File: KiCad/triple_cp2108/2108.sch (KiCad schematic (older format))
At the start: 79 parts, among them IC1 CP2108-B03-GMR, J19 Screw_Terminal_01x09, J20 Screw_Terminal_01x09, J21 Screw_Terminal_01x09, J22 Screw_Terminal_01x09, J23 RJ12, J24 RJ12, J25 RJ12, J26 RJ12, J28 DB9_Male, J29 DB9_Male, J30 DB9_Male, J31 DB9_Male, U11 SP3243, U12 SP3243, U13 SP3243, U14 SP3243

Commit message: Netlist generated
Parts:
- removed J19, J20, J21, J22: Screw_Terminal_01x09, Connector_PinHeader_1.00mm:PinHeader_1x09_P1.00mm_Horizontal, symbol Connector:Screw_Terminal_01x09
- C11: renamed from C69; footprint (none) -> Capacitor_SMD:C_0805_2012Metric_Pad1.18x1.45mm_HandSolder
- C16: renamed from C71; footprint (none) -> Capacitor_SMD:C_0805_2012Metric_Pad1.18x1.45mm_HandSolder
- C9: renamed from C67; footprint (none) -> Capacitor_SMD:C_0805_2012Metric_Pad1.18x1.45mm_HandSolder
- J4: renamed from J23; footprint (none) -> Connector_RJ:RJ12_Amphenol_54601
- J5: renamed from J25; footprint (none) -> Connector_RJ:RJ12_Amphenol_54601
- J6: renamed from J24; footprint (none) -> Connector_RJ:RJ12_Amphenol_54601
- J7: renamed from J26; footprint (none) -> Connector_RJ:RJ12_Amphenol_54601
- R10: renamed from R57; footprint Resistor_SMD:R_1206_3216Metric -> Resistor_SMD:R_0805_2012Metric_Pad1.20x1.40mm_HandSolder
- R11: renamed from R74; footprint Resistor_SMD:R_1206_3216Metric -> Resistor_SMD:R_0805_2012Metric_Pad1.20x1.40mm_HandSolder
- R12: renamed from R58; footprint Resistor_SMD:R_1206_3216Metric -> Resistor_SMD:R_0805_2012Metric_Pad1.20x1.40mm_HandSolder
- R13: renamed from R75; footprint Resistor_SMD:R_1206_3216Metric -> Resistor_SMD:R_0805_2012Metric_Pad1.20x1.40mm_HandSolder
- R14: renamed from R59; footprint Resistor_SMD:R_1206_3216Metric -> Resistor_SMD:R_0805_2012Metric_Pad1.20x1.40mm_HandSolder
- R15: renamed from R76; footprint Resistor_SMD:R_1206_3216Metric -> Resistor_SMD:R_0805_2012Metric_Pad1.20x1.40mm_HandSolder
- R16: renamed from R60; footprint Resistor_SMD:R_1206_3216Metric -> Resistor_SMD:R_0805_2012Metric_Pad1.20x1.40mm_HandSolder
- R17: renamed from R77; footprint Resistor_SMD:R_1206_3216Metric -> Resistor_SMD:R_0805_2012Metric_Pad1.20x1.40mm_HandSolder
- R18: renamed from R61; footprint Resistor_SMD:R_1206_3216Metric -> Resistor_SMD:R_0805_2012Metric_Pad1.20x1.40mm_HandSolder
- R19: renamed from R78; footprint Resistor_SMD:R_1206_3216Metric -> Resistor_SMD:R_0805_2012Metric_Pad1.20x1.40mm_HandSolder
- R20: renamed from R62; footprint Resistor_SMD:R_1206_3216Metric -> Resistor_SMD:R_0805_2012Metric_Pad1.20x1.40mm_HandSolder
- R21: renamed from R79; footprint Resistor_SMD:R_1206_3216Metric -> Resistor_SMD:R_0805_2012Metric_Pad1.20x1.40mm_HandSolder
- R22: renamed from R64; value R -> 100; footprint Resistor_SMD:R_1206_3216Metric -> Resistor_SMD:R_0805_2012Metric_Pad1.20x1.40mm_HandSolder
- R23: renamed from R65; value R -> 100; footprint Resistor_SMD:R_1206_3216Metric -> Resistor_SMD:R_0805_2012Metric_Pad1.20x1.40mm_HandSolder
- R24: renamed from R66; value R -> 100; footprint Resistor_SMD:R_1206_3216Metric -> Resistor_SMD:R_0805_2012Metric_Pad1.20x1.40mm_HandSolder
- R25: renamed from R67; value R -> 100; footprint Resistor_SMD:R_1206_3216Metric -> Resistor_SMD:R_0805_2012Metric_Pad1.20x1.40mm_HandSolder
- R26: renamed from R68; value R -> 100; footprint Resistor_SMD:R_1206_3216Metric -> Resistor_SMD:R_0805_2012Metric_Pad1.20x1.40mm_HandSolder
- R27: renamed from R69; value R -> 100; footprint Resistor_SMD:R_1206_3216Metric -> Resistor_SMD:R_0805_2012Metric_Pad1.20x1.40mm_HandSolder
- R28: renamed from R70; value R -> 100; footprint Resistor_SMD:R_1206_3216Metric -> Resistor_SMD:R_0805_2012Metric_Pad1.20x1.40mm_HandSolder
- R29: renamed from R71; value R -> 100; footprint Resistor_SMD:R_1206_3216Metric -> Resistor_SMD:R_0805_2012Metric_Pad1.20x1.40mm_HandSolder
- R5: renamed from R55; footprint Resistor_SMD:R_1206_3216Metric -> Resistor_SMD:R_0805_2012Metric_Pad1.20x1.40mm_HandSolder
- R6: renamed from R72; footprint Resistor_SMD:R_1206_3216Metric -> Resistor_SMD:R_0805_2012Metric_Pad1.20x1.40mm_HandSolder
- R7: renamed from R63; footprint Resistor_SMD:R_1206_3216Metric -> Resistor_SMD:R_0805_2012Metric_Pad1.20x1.40mm_HandSolder
- R8: renamed from R56; footprint Resistor_SMD:R_1206_3216Metric -> Resistor_SMD:R_0805_2012Metric_Pad1.20x1.40mm_HandSolder
- R9: renamed from R73; footprint Resistor_SMD:R_1206_3216Metric -> Resistor_SMD:R_0805_2012Metric_Pad1.20x1.40mm_HandSolder
- U3: renamed from U11; Manufacturer_Part_Number (none) -> SP3243EUEY-L/TR; Mouser Price/Stock (none) -> https://lcsc.com/product-detail/RS232-ICs_MaxLinear_SP3243E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
- U4: renamed from U12; Manufacturer_Part_Number (none) -> SP3243EUEY-L/TR; Mouser Price/Stock (none) -> https://lcsc.com/product-detail/RS232-ICs_MaxLinear_SP3243E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
- U5: renamed from U13; Manufacturer_Part_Number (none) -> SP3243EUEY-L/TR; Mouser Price/Stock (none) -> https://lcsc.com/product-detail/RS232-ICs_MaxLinear_SP3243E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
- U6: renamed from U14; Manufacturer_Part_Number (none) -> SP3243EUEY-L/TR; Mouser Price/Stock (none) -> https://lcsc.com/product-detail/RS232-ICs_MaxLinear_SP3243E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
- renumbered C68 to C10, C72 to C12, C73 to C13, C74 to C14, C70 to C15, C75 to C17, C76 to C18, C77 to C19, C78 to C20, C79 to C21, C80 to C22, C81 to C23, C82 to C24, C83 to C25, C84 to C26, C85 to C27, C86 to C28, C87 to C29, C88 to C30, C89 to C31, C90 to C32, C91 to C33, C92 to C34, C93 to C35, C94 to C36, C66 to C8, D19 to D13, D20 to D14, D21 to D15, D22 to D16, D23 to D17, D24 to D18, D25 to D19, D26 to D20, J30 to J10, J31 to J11, J28 to J8, J29 to J9
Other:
- moved on the sheet: J4, J5, J6, J7, R10, R11, R12, R13, R14, R15, R16, R17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

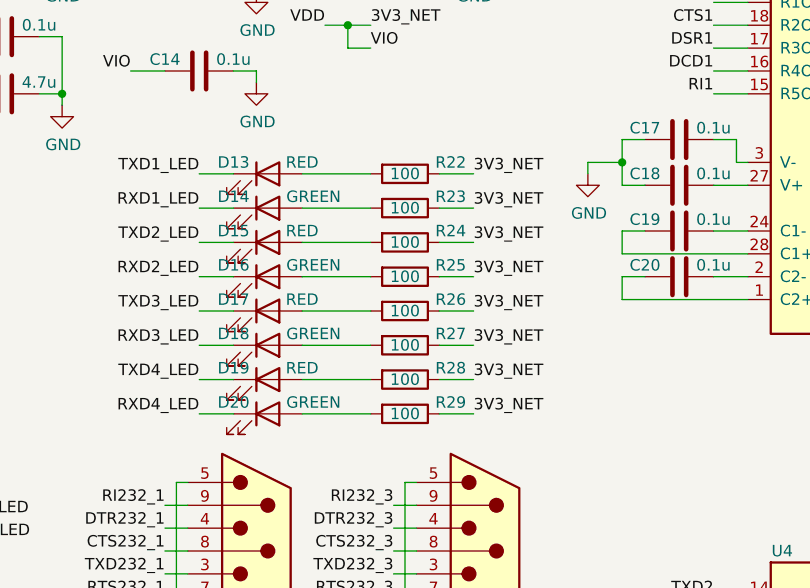
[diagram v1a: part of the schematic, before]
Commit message: LED resis val changed
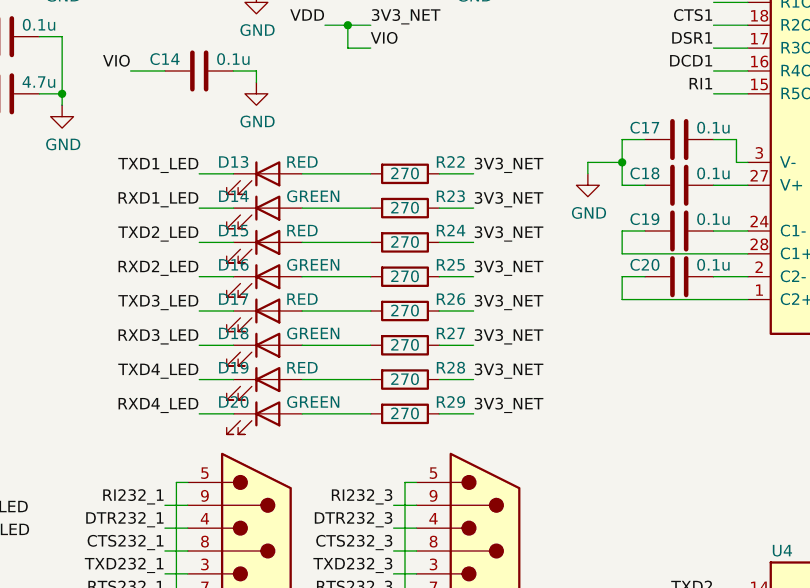
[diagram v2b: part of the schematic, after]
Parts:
- R22, R23, R24, R25, R26, R27, R28, R29: value 100 -> 270
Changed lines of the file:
@@
 AR Path="/60246936/604C02CA" Ref="R72"  Part="1"
 F 0 "R22" V 5150 2100 50  0000 C CNN
-F 1 "100" V 5200 1900 50  0000 C CNN
+F 1 "270" V 5200 1900 50  0000 C CNN
 F 2 "Resistor_SMD:R_0805_2012Metric_Pad1.20x1.40mm_HandSolder" V 5130 1900 50  0001 C CNN
 F 3 "~" H 5200 1900 50  0001 C CNN
@@
 AR Path="/60246936/60572F1D" Ref="R73"  Part="1"
 F 0 "R23" V 5150 2250 50  0000 C CNN
-F 1 "100" V 5200 2050 50  0000 C CNN
+F 1 "270" V 5200 2050 50  0000 C CNN
 F 2 "Resistor_SMD:R_0805_2012Metric_Pad1.20x1.40mm_HandSolder" V 5130 2050 50  0001 C CNN
 F 3 "~" H 5200 2050 50  0001 C CNN
@@
 AR Path="/60246936/6062BE20" Ref="R74"  Part="1"
 F 0 "R24" V 5150 2400 50  0000 C CNN
-F 1 "100" V 5200 2200 50  0000 C CNN
+F 1 "270" V 5200 2200 50  0000 C CNN
 F 2 "Resistor_SMD:R_0805_2012Metric_Pad1.20x1.40mm_HandSolder" V 5130 2200 50  0001 C CNN
 F 3 "~" H 5200 2200 50  0001 C CNN
@@
 AR Path="/60246936/6062BE30" Ref="R75"  Part="1"
 F 0 "R25" V 5150 2550 50  0000 C CNN
-F 1 "100" V 5200 2350 50  0000 C CNN
+F 1 "270" V 5200 2350 50  0000 C CNN
 F 2 "Resistor_SMD:R_0805_2012Metric_Pad1.20x1.40mm_HandSolder" V 5130 2350 50  0001 C CNN
 F 3 "~" H 5200 2350 50  0001 C CNN
@@
 AR Path="/60246936/6065BC30" Ref="R76"  Part="1"
 F 0 "R26" V 5150 2700 50  0000 C CNN
-F 1 "100" V 5200 2500 50  0000 C CNN
+F 1 "270" V 5200 2500 50  0000 C CNN
 F 2 "Resistor_SMD:R_0805_2012Metric_Pad1.20x1.40mm_HandSolder" V 5130 2500 50  0001 C CNN
 F 3 "~" H 5200 2500 50  0001 C CNN
@@
 AR Path="/60246936/6065BC40" Ref="R77"  Part="1"
 F 0 "R27" V 5150 2850 50  0000 C CNN
-F 1 "100" V 5200 2650 50  0000 C CNN
+F 1 "270" V 5200 2650 50  0000 C CNN
 F 2 "Resistor_SMD:R_0805_2012Metric_Pad1.20x1.40mm_HandSolder" V 5130 2650 50  0001 C CNN
 F 3 "~" H 5200 2650 50  0001 C CNN
@@
 AR Path="/60246936/6068CF47" Ref="R78"  Part="1"
 F 0 "R28" V 5150 3000 50  0000 C CNN
-F 1 "100" V 5200 2800 50  0000 C CNN
+F 1 "270" V 5200 2800 50  0000 C CNN
 F 2 "Resistor_SMD:R_0805_2012Metric_Pad1.20x1.40mm_HandSolder" V 5130 2800 50  0001 C CNN
 F 3 "~" H 5200 2800 50  0001 C CNN
@@
 AR Path="/60246936/6068CF57" Ref="R79"  Part="1"
 F 0 "R29" V 5150 3150 50  0000 C CNN
-F 1 "100" V 5200 2950 50  0000 C CNN
+F 1 "270" V 5200 2950 50  0000 C CNN
 F 2 "Resistor_SMD:R_0805_2012Metric_Pad1.20x1.40mm_HandSolder" V 5130 2950 50  0001 C CNN
 F 3 "~" H 5200 2950 50  0001 C CNN

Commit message: layout in prgs
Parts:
- J10, J11, J8, J9: footprint Connector_Dsub:DSUB-9_Male_EdgeMount_P2.77mm -> Connector_Dsub:DSUB-9_Male_Vertical_P2.77x2.84mm
- J4, J7: value RJ12 -> RJ25; footprint Connector_RJ:RJ12_Amphenol_54601 -> Connector_RJ:RJ25_Wayconn_MJEA-660X1_Horizontal
- J5: renamed from J6; value RJ12 -> RJ25; footprint Connector_RJ:RJ12_Amphenol_54601 -> Connector_RJ:RJ25_Wayconn_MJEA-660X1_Horizontal
- J6: renamed from J5; value RJ12 -> RJ25; footprint Connector_RJ:RJ12_Amphenol_54601 -> Connector_RJ:RJ25_Wayconn_MJEA-660X1_Horizontal
- renumbered R14 to R10, R16 to R11, R18 to R12, R20 to R13, R6 to R14, R9 to R15, R11 to R16, R13 to R17, R15 to R18, R17 to R19, R19 to R20, R7 to R6, R8 to R7, R10 to R8, R12 to R9
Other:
- moved on the sheet: J6, J7, R14, R15, R16, R17, R18, R19, R20, R21

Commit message: 1
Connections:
- net RXD3_LED: no longer IC1.23 (GPIO.13)
- net RXD4_LED: now also IC1.23 (GPIO.13)
- net TXD3_LED: no longer IC1.26 (GPIO.12)
- net TXD4_LED: now also IC1.26 (GPIO.12)
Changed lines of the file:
@@
 RXD3_LED
 Text Label 2050 5150 3    50   ~ 0
-TXD3_LED
+TXD4_LED
 Text Label 1750 5150 3    50   ~ 0
-RXD3_LED
+RXD4_LED
 Wire Wire Line
 	2050 5150 2050 5000
